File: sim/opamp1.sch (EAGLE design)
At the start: 7 parts, among them X1 OPAMP

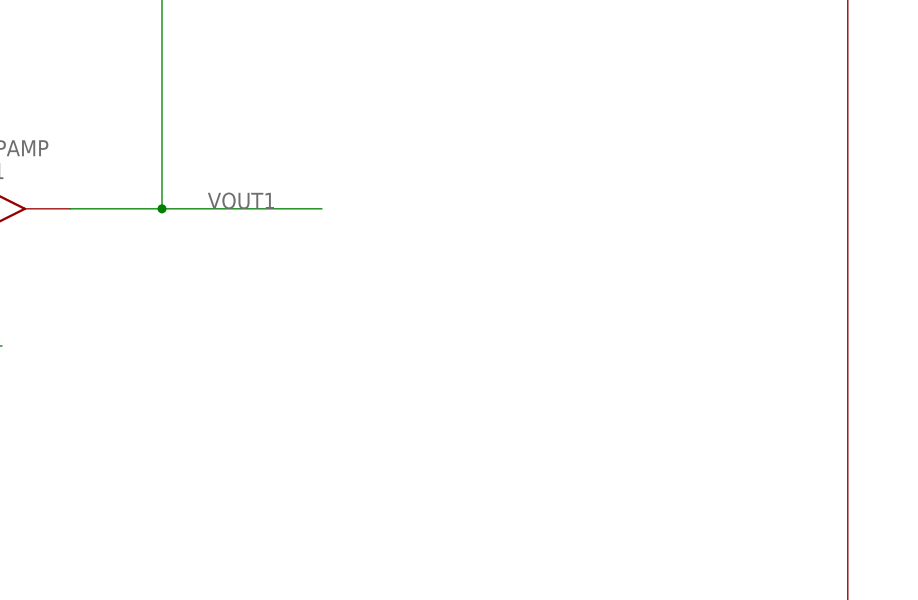
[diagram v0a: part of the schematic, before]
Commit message: added diode distortion sim
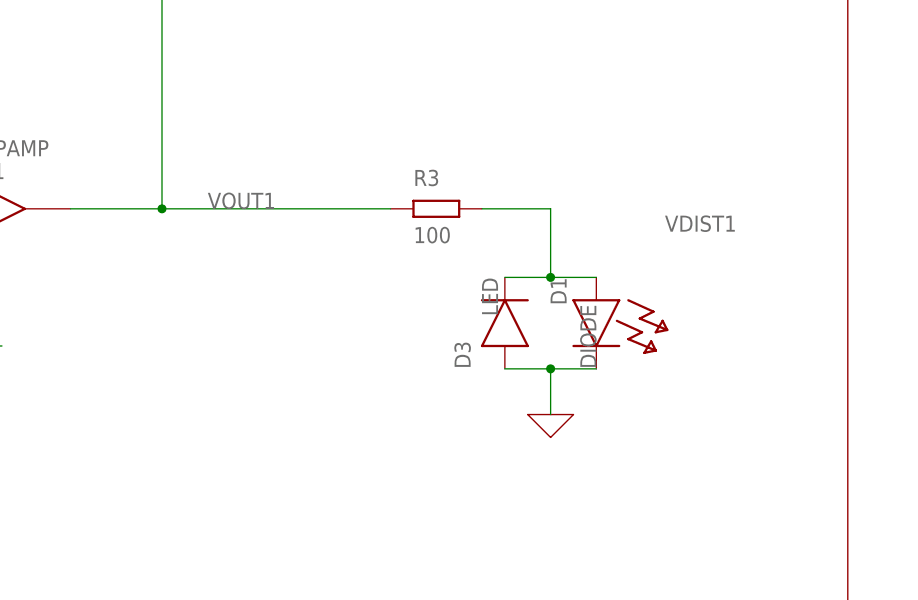
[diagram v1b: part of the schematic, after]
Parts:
- added D1: LED, ngspice-simulation:LED
- added D3: DIODE, ngspice-simulation:DIODE
- added R3: 100, ngspice-simulation:R
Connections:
- new net VDIST1: D1.A, D3.C, R3.2
- net 0: now also D1.C, D3.A
- net VOUT1: now also R3.1
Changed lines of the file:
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@@
 <part name="X1" library="ngspice-simulation" library_urn="urn:adsk.eagle:library:5272020" deviceset="OPAMP" device=""/>
 <part name="C3" library="ngspice-simulation" library_urn="urn:adsk.eagle:library:5272020" deviceset="C" device="" value="100p"/>
+<part name="R3" library="ngspice-simulation" library_urn="urn:adsk.eagle:library:527439" deviceset="R" device="" value="100"/>
+<part name="X_4" library="ngspice-simulation" library_urn="urn:adsk.eagle:library:5272020" deviceset="GND" device=""/>
+<part name="D3" library="ngspice-simulation" library_urn="urn:adsk.eagle:library:527439" deviceset="DIODE" device=""/>
+<part name="D1" library="ngspice-simulation" library_urn="urn:adsk.eagle:library:527439" deviceset="LED" device=""/>
 </parts>
 <sheets>
@@
 <attribute name="NAME" x="142.24" y="149.86" size="1.778" layer="95" rot="R90"/>
 <attribute name="VALUE" x="144.78" y="149.86" size="1.778" layer="96" rot="R90"/>
+</instance>
+<instance part="R3" gate="G$1" x="187.96" y="111.76" smashed="yes">
+<attribute name="NAME" x="185.42" y="114.3" size="1.778" layer="95"/>
+<attribute name="VALUE" x="185.42" y="107.95" size="1.778" layer="96"/>
+</instance>
+<instance part="X_4" gate="G$1" x="200.66" y="88.9" smashed="yes"/>
+<instance part="D3" gate="G$1" x="195.58" y="99.06" smashed="yes" rot="R90">
+<attribute name="NAME" x="191.77" y="93.98" size="1.778" layer="95" rot="R90"/>
+<attribute name="VALUE" x="205.74" y="93.98" size="1.778" layer="96" rot="R90"/>
+</instance>
+<instance part="D1" gate="G$1" x="205.74" y="99.06" smashed="yes" rot="R270">
+<attribute name="NAME" x="200.66" y="104.14" size="1.778" layer="95" rot="R270"/>
+<attribute name="VALUE" x="193.04" y="104.14" size="1.778" layer="96" rot="R270"/>
 </instance>
 </instances>
@@
 <wire x1="157.48" y1="111.76" x2="147.32" y2="111.76" width="0.1524" layer="91"/>
 <label x="162.56" y="111.76" size="1.778" layer="95"/>
-<wire x1="157.48" y1="111.76" x2="175.26" y2="111.76" width="0.1524" layer="91"/>
+<wire x1="157.48" y1="111.76" x2="182.88" y2="111.76" width="0.1524" layer="91"/>
 <junction x="157.48" y="111.76"/>
 <pinref part="X1" gate="G$1" pin="VOUT"/>
@@
 <wire x1="157.48" y1="147.32" x2="149.86" y2="147.32" width="0.1524" layer="91"/>
 <junction x="157.48" y="142.24"/>
+<pinref part="R3" gate="G$1" pin="1"/>
 </segment>
 </net>
@@
 <pinref part="X1" gate="G$1" pin="P"/>
 </segment>
+<segment>
+<wire x1="195.58" y1="93.98" x2="200.66" y2="93.98" width="0.1524" layer="91"/>
+<pinref part="X_4" gate="G$1" pin="0"/>
+<wire x1="200.66" y1="93.98" x2="205.74" y2="93.98" width="0.1524" layer="91"/>
+<wire x1="200.66" y1="93.98" x2="200.66" y2="88.9" width="0.1524" layer="91"/>
+<junction x="200.66" y="93.98"/>
+<pinref part="D3" gate="G$1" pin="A"/>
+<pinref part="D1" gate="G$1" pin="C"/>
+</segment>
 </net>
 <net name="VSS" class="0">
@@
 </segment>
 </net>
+<net name="VDIST1" class="0">
+<segment>
+<pinref part="R3" gate="G$1" pin="2"/>
+<wire x1="193.04" y1="111.76" x2="200.66" y2="111.76" width="0.1524" layer="91"/>
+<wire x1="200.66" y1="111.76" x2="200.66" y2="104.14" width="0.1524" layer="91"/>
+<wire x1="200.66" y1="104.14" x2="205.74" y2="104.14" width="0.1524" layer="91"/>
+<wire x1="200.66" y1="104.14" x2="195.58" y2="104.14" width="0.1524" layer="91"/>
+<junction x="200.66" y="104.14"/>
+<probe x="208.28" y="114.3" size="1.778" layer="89" probetype="0"/>
+<label x="213.36" y="109.22" size="1.778" layer="95"/>
+<pinref part="D3" gate="G$1" pin="C"/>
+<pinref part="D1" gate="G$1" pin="A"/>
+</segment>
+</net>
